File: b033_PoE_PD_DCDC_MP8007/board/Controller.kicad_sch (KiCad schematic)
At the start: 25 parts, among them U1 MP8007, U2 POE70P-50L

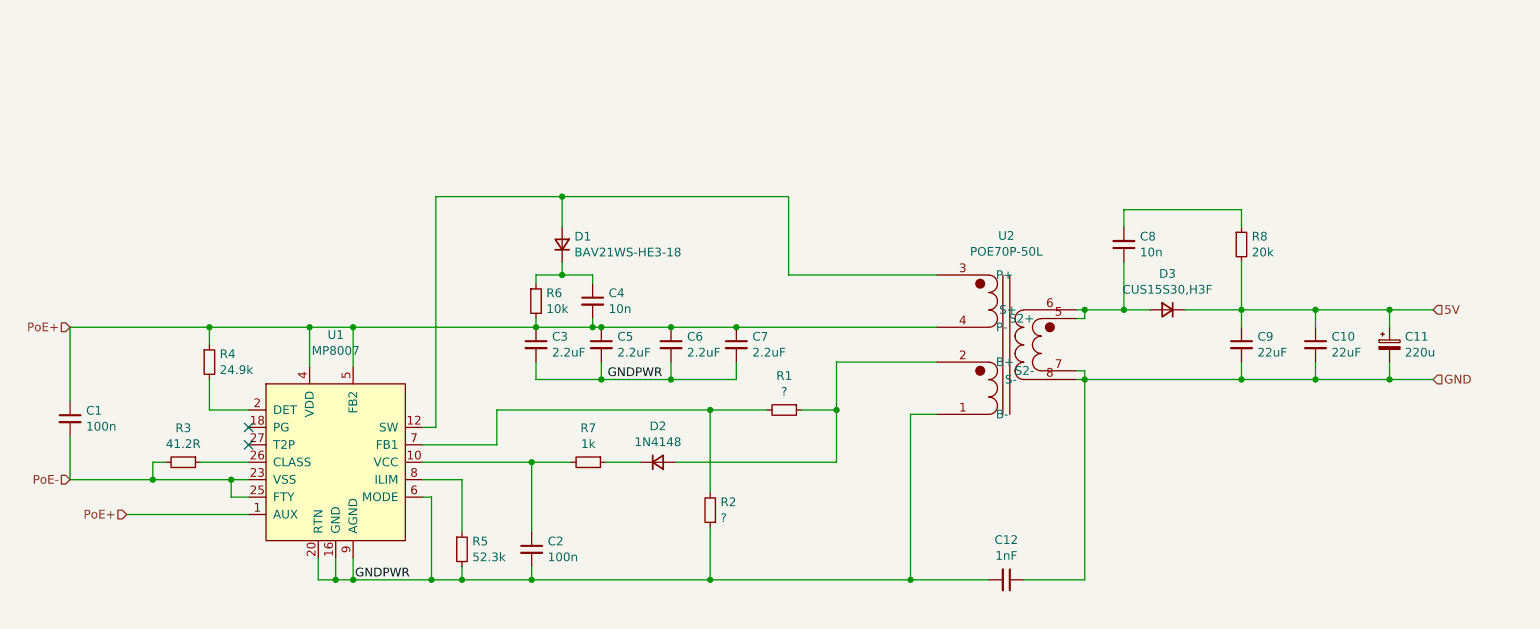
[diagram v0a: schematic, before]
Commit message: changed coil to POE30P
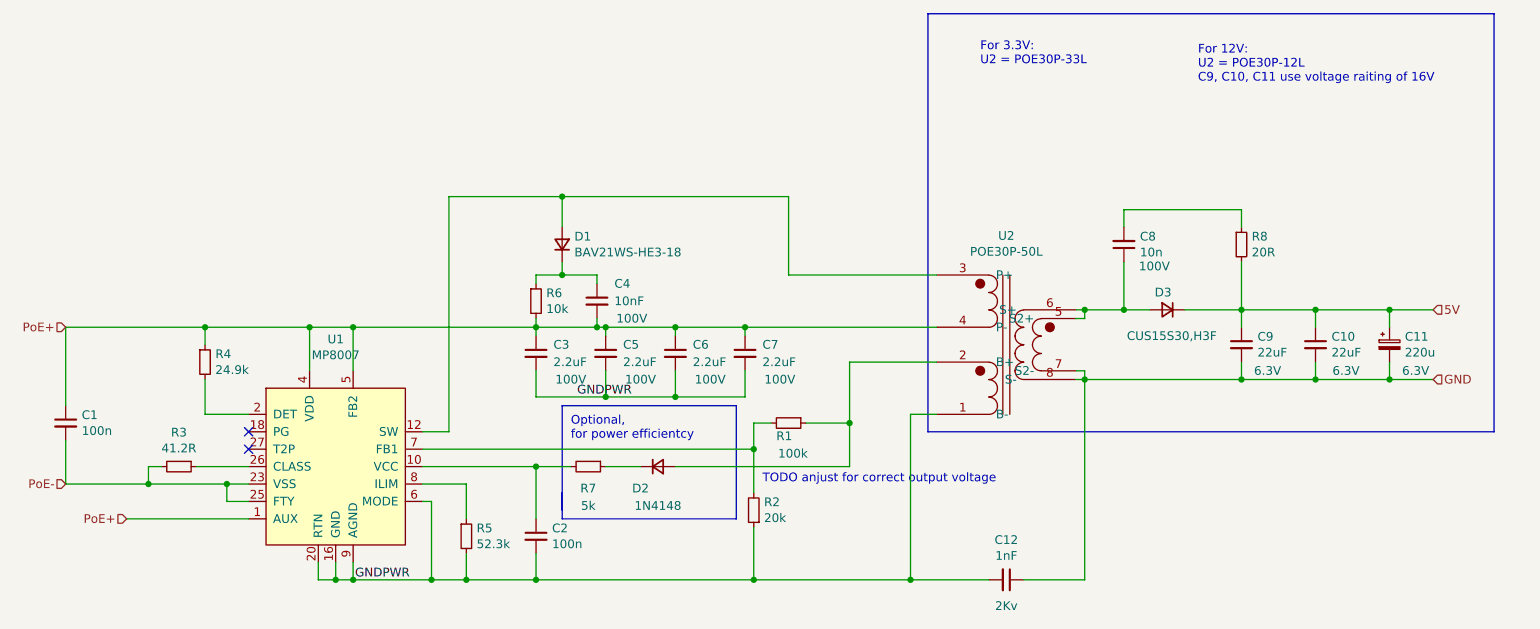
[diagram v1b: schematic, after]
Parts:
- C10, C11, C9: Voltage (none) -> 6.3V
- C12: Voltage (none) -> 2Kv
- C3, C5, C6, C7, C8: Voltage (none) -> 100V
- C4: value 10n -> 10nF; Voltage (none) -> 100V
- R1: value ? -> 100k
- R2: value ? -> 20k
- R7: value 1k -> 5k
- R8: value 20k -> 20R
- U2: value POE70P-50L -> POE30P-50L; footprint local:Transformer_Coilcraft_POE70P -> local:Transformer_Coilcraft_POE30P
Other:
- note added: "For 12V: U2 = POE30P-12L C9, C10, C11 use voltage raiting of 16V"
- note added: "For 3.3V: U2 = POE30P-33L"
- note added: "Optional, for power efficientcy"
- note added: "TODO anjust for correct output voltage"
- moved on the sheet: C1, C2, C3, C4, C5, C6, C7, D2, R1, R2, R3, R4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
